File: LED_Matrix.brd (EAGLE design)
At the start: 74.6 x 29.2 mm, 48 parts, among them IC1 KF33, J1 DCJ0202, Q1 16MHz

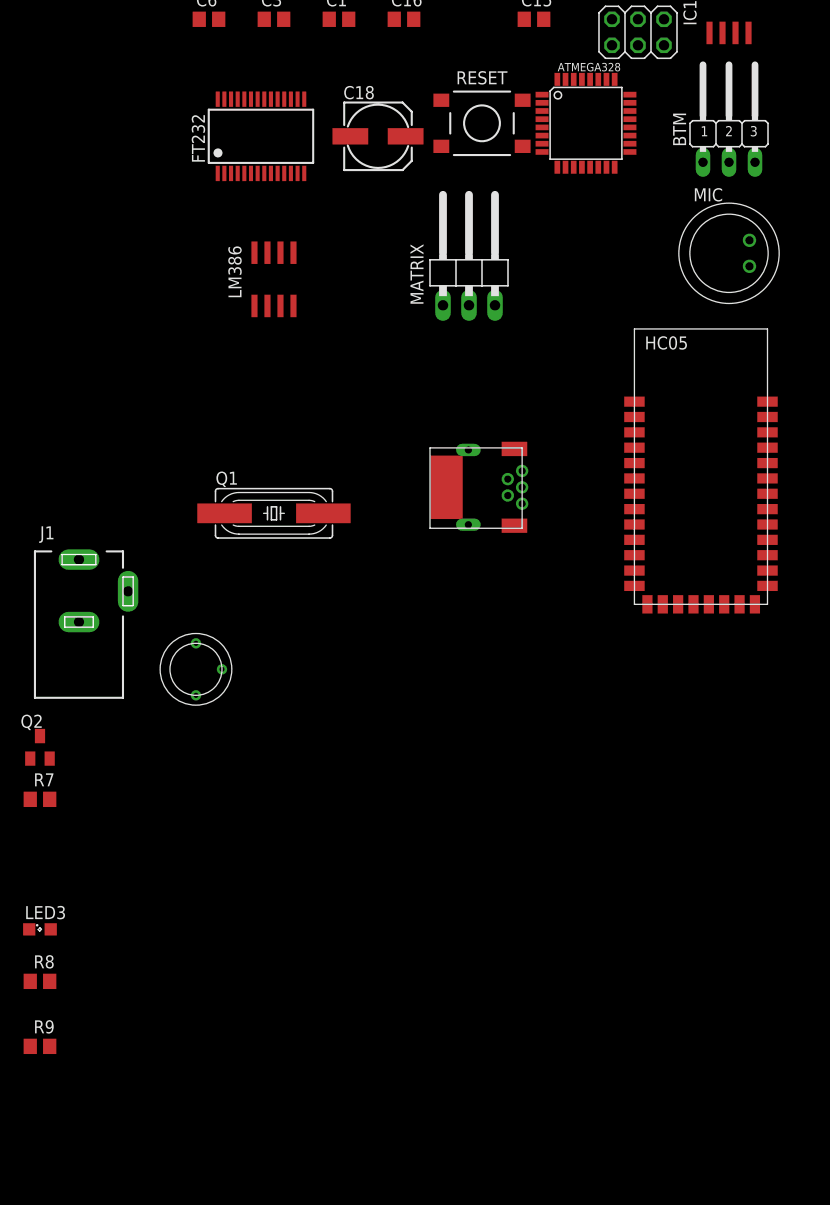
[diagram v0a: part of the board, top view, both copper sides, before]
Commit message: analog switch added
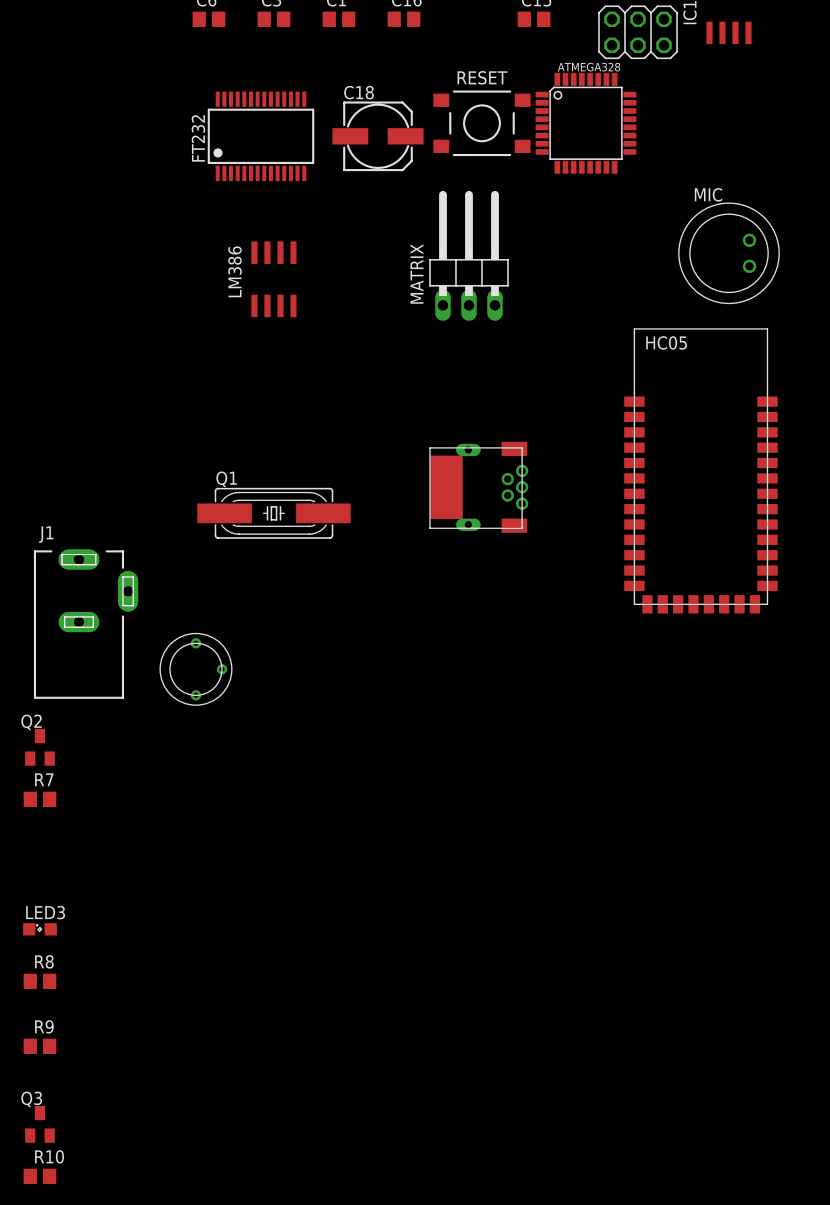
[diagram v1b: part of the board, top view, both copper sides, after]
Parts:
- removed BTM: (no value), jumper:JP2W
- added Q3: (no value), semicon-smd-ipc:SOT23
- added R10: 1k, rcl:R0805
- R7: value 10k -> 1k
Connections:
- removed net N$10: BTM.1, R4.2
- new net N$27: Q3.1, R10.2
- net BTM_MODESELECT: now also Q3.3, R10.1, R4.2; no longer BTM.2
- net GND: now also Q3.2; no longer BTM.3
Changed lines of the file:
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@@
 <element name="LM386" library="debegr92" package="SO08" value="LM386SO08" x="-62.23" y="33.02"/>
 <element name="ISP" library="pinhead" package="2X03" value="" x="-26.67" y="57.15"/>
-<element name="BTM" library="jumper" package="JP2W" value="" x="-17.78" y="45.72"/>
 <element name="LED1" library="led" package="SML0805" value="" x="-22.86" y="78.74"/>
 <element name="LED2" library="led" package="SML0805" value="" x="-29.21" y="78.74"/>
@@
 </element>
 <element name="Q2" library="semicon-smd-ipc" package="SOT23" value="" x="-85.09" y="-12.7"/>
-<element name="R7" library="rcl" package="R0805" value="10k" x="-85.09" y="-17.78"/>
+<element name="R7" library="rcl" package="R0805" value="1k" x="-85.09" y="-17.78"/>
 <element name="LED3" library="led" package="SML0805" value="" x="-85.09" y="-30.48"/>
 <element name="R8" library="rcl" package="R0805" value="470" x="-85.09" y="-35.56"/>
 <element name="R9" library="rcl" package="R0805" value="470" x="-85.09" y="-41.91"/>
+<element name="Q3" library="semicon-smd-ipc" package="SOT23" value="" x="-85.09" y="-49.53"/>
+<element name="R10" library="rcl" package="R0805" value="1k" x="-85.09" y="-54.61"/>
 </elements>
 <signals>
@@
 <contactref element="HC05" pad="21"/>
 <contactref element="R3" pad="1"/>
-<contactref element="BTM" pad="3"/>
 <contactref element="FT232" pad="25"/>
 <contactref element="FT232" pad="7"/>
@@
 <contactref element="R8" pad="1"/>
 <contactref element="R9" pad="1"/>
+<contactref element="Q3" pad="2"/>
 <contactref element="HC05" pad="22"/>
+<wire x1="-86.04" y1="-41.91" x2="-84.14" y2="-50.63" width="0" layer="19" extent="1-1"/>
 <wire x1="-86.04" y1="-35.56" x2="-86.04" y2="-41.91" width="0" layer="19" extent="1-1"/>
 <wire x1="-84.14" y1="-13.8" x2="-86.04" y2="-35.56" width="0" layer="19" extent="1-1"/>
@@
 <wire x1="-45.885" y1="46.01" x2="-37.935" y2="46.01" width="0" layer="19" extent="1-1"/>
 <wire x1="-27.4574" y1="48.66" x2="-36.0426" y2="49.46" width="0" layer="19" extent="1-1"/>
-<wire x1="-15.24" y1="44.45" x2="-17.145" y2="57.09" width="0" layer="19" extent="1-1"/>
-<wire x1="-15.78" y1="36.83" x2="-15.24" y2="44.45" width="0" layer="19" extent="1-1"/>
 <wire x1="-45.72" y1="30.48" x2="-60.325" y2="30.42" width="0" layer="19" extent="1-1"/>
+<wire x1="-15.78" y1="36.83" x2="-27.4574" y2="48.66" width="0" layer="19" extent="1-1"/>
 <wire x1="-37.99" y1="14.3" x2="-45.72" y2="30.48" width="0" layer="19" extent="1-1"/>
 <wire x1="-27.02" y1="3.07" x2="-37.99" y2="14.3" width="0" layer="19" extent="1-1"/>
@@
 </signal>
 <signal name="BTM_MODESELECT">
-<contactref element="BTM" pad="2"/>
 <contactref element="HC05" pad="34"/>
 <contactref element="ATMEGA328" pad="13"/>
-<wire x1="-31.35" y1="43.9674" x2="-17.78" y2="44.45" width="0" layer="19" extent="1-1"/>
-<wire x1="-14.02" y1="21.07" x2="-17.78" y2="44.45" width="0" layer="19" extent="1-1"/>
-</signal>
-<signal name="N$10">
-<contactref element="BTM" pad="1"/>
+<contactref element="R10" pad="1"/>
 <contactref element="R4" pad="2"/>
-<wire x1="-20.32" y1="44.45" x2="-30.8" y2="73.66" width="0" layer="19" extent="1-1"/>
+<contactref element="Q3" pad="3"/>
+<wire x1="-85.09" y1="-48.43" x2="-86.04" y2="-54.61" width="0" layer="19" extent="1-1"/>
+<wire x1="-14.02" y1="21.07" x2="-85.09" y2="-48.43" width="0" layer="19" extent="1-1"/>
+<wire x1="-31.35" y1="43.9674" x2="-14.02" y2="21.07" width="0" layer="19" extent="1-1"/>
+<wire x1="-30.8" y1="73.66" x2="-31.35" y2="43.9674" width="0" layer="19" extent="1-1"/>
 </signal>
 <signal name="N$9">
@@
 <wire x1="-14.02" y1="6.07" x2="-84.04" y2="-30.48" width="0" layer="19" extent="1-1"/>
 </signal>
+<signal name="N$27">
+<contactref element="R10" pad="2"/>
+<contactref element="Q3" pad="1"/>
+<wire x1="-86.04" y1="-50.63" x2="-84.14" y2="-54.61" width="0" layer="19" extent="1-1"/>
+</signal>
 </signals>

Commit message: return point
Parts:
- removed JRX, JTX: (no value), jumper:SJ_2
- added LEDON: (no value), led:SML0805
- added R11, R12, R13: 470, rcl:R0805
- added U$1: DG2016, Tobias:MSOP10
- C18: device rcl:153CLV-0605 -> rcl:E2,5-7
- MATRIX: device pinhead:1X03/90 -> pinhead:1X03
- moved R10 162.9 mm to (54.6, 29.2)
- moved Q3 159.6 mm to (55.9, 25.4), turned to 90 degrees
- moved R9 157.8 mm to (44.5, 48.3)
- moved R8 154.9 mm to (62.9, 10.2), flipped to the bottom, turned to 90 degrees
- moved LED3 150.7 mm to (55.9, 22.9)
- moved Q2 139.9 mm to (53.3, 7.62), turned to 270 degrees
- moved R7 137.8 mm to (49.5, 11.4)
- moved C5 115.9 mm to (48.3, 25.4), flipped to the bottom, turned to 90 degrees
- moved C19 113.1 mm to (35.6, 20.3), flipped to the bottom, turned to 270 degrees
- moved R4 112.3 mm to (57.1, 5.08), turned to 90 degrees
- moved Q1 107.8 mm to (44.5, 25.4), turned to 180 degrees
- moved LED2 107.7 mm to (55.9, 12.7)
- moved C9 105.9 mm to (54.6, 2.54), turned to 270 degrees
- moved C4 104.5 mm to (40.6, 25.4), flipped to the bottom, turned to 270 degrees
- moved LM386 104.1 mm to (38.1, 5.08)
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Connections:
- new net N$10: LEDON.C, R11.2
- new net N$26: HC05.2, R12.1, R13.2
- new net N$28: ATMEGA328.32, U$1.1
- new net N$29: ATMEGA328.1, U$1.5
- net +5V: now also LEDON.A, U$1.8
- net GND: now also R11.1, R13.1, U$1.3
- net N$12: now also U$1.10; no longer JTX.2
- net N$15: now also U$1.6; no longer JRX.2
- net RX_BTM: now also R12.2, U$1.9; no longer HC05.2, JRX.1
- net RX_FT232: now also U$1.2; no longer JRX.3
- net TX_BTM: now also U$1.7; no longer JTX.1
- net TX_FT232: now also U$1.4; no longer JTX.3
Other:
- board size 74.6 x 29.2 mm -> 74.6 x 30.5 mm

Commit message: version 2 Final
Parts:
- removed C15: 100n, rcl:C0805
- removed C16: 47n, rcl:C0805
- removed C17: 10u, rcl:C0805
- removed C18: 250u, rcl:E2,5-7
- removed C19: 470n, rcl:C0805
- removed C4, C5: 22p, rcl:C0805
- removed IC1: KF33, debegr92:SO08
- removed LEDON: (no value), led:SML0805
- removed LM386: LM386SO08, debegr92:SO08
- removed MATRIX: (no value), pinhead:1X03
- removed MIC: MIC_EMY-9765PEMY-9765P, debegr92:MIC
- removed Q1: 16MHz, crystal:HC49UP
- removed R6: 10, rcl:R0805
- removed TRIMMER: 10k, Tobias:T7YA
- removed U$1: DG2016, Tobias:MSOP10
- added D1: (no value), led:SML0805
- added DG2016: DG2016, Tobias:MSOP10
- added KF33: KF33, debegr92:SO08
- added MTX: (no value), pinhead:1X03
- added Q4: CSTCR6M00G53Z, murata-filter:CSTCR6M
- added SJ1: (no value), jumper:SJ
- moved C3 120.3 mm to (45.7, 5.40), turned to 90 degrees
- moved R5 115.0 mm to (54.3, 3.49), turned to 270 degrees
- moved C6 99.6 mm to (17.8, 8.89), flipped to the bottom, turned to 90 degrees
- moved C7 70.5 mm to (11.4, 2.54), turned to 270 degrees
- moved R13 39.7 mm to (31.1, 24.4), turned to 180 degrees
- moved R9 37.6 mm to (52.1, 11.4), turned to 180 degrees
- moved R12 36.7 mm to (31.1, 21.9), turned to 0 degrees
- moved HC05 28.0 mm to (39.4, 23.8), turned to 270 degrees
- moved R10 24.1 mm to (36.5, 13.3), turned to 270 degrees
- moved Q3 20.4 mm to (39.4, 13.3), turned to 0 degrees
- moved ATMEGA328 14.6 mm to (32.1, 6.99), turned to 0 degrees
- moved R3 14.5 mm to (52.1, 15.9), flipped to the top, turned to 180 degrees
- moved RESET 13.7 mm to (5.40, 28.3)
- moved LED3 13.1 mm to (47.9, 12.4), turned to 180 degrees
- moved C12 11.7 mm to (22.9, 12.7), flipped to the top, turned to 0 degrees
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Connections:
- removed net N$16: C19.1, MIC.TERMINAL1, TRIMMER.B
- removed net N$17: C17.2, LM386.8
- removed net N$18: C16.2, R6.1
- removed net N$20: C17.1, LM386.1
- removed net N$21: C16.1, C18.+, LM386.5
- removed net N$22: C19.2, LM386.3
- net +3V3: now also KF33.1; no longer IC1.1
- net +5V: now also D1.A, DG2016.8, KF33.8, MTX.3, SJ1.2; no longer IC1.8, LEDON.A, LM386.6, MATRIX.3, TRIMMER.A, U$1.8, USB.5, USB.GND, USB.GND1, USB.GND3, USB.GND4, USB.GND5
- net AUDIO_IN: no longer C18.-
- net GND: now also DG2016.3, KF33.2, KF33.3, KF33.6, KF33.7, MTX.1, Q4.2, USB.5, USB.GND, USB.GND1, USB.GND3, USB.GND4, USB.GND5; no longer C15.2, C4.1, C5.1, IC1.2, IC1.3, IC1.6, IC1.7, LM386.2, LM386.4, MATRIX.1, MIC.TERMINAL2, R6.2, TRIMMER.C, U$1.3, USB.1
- net N$10: now also D1.C; no longer LEDON.C
- net N$12: now also DG2016.10; no longer U$1.10
- net N$15: now also DG2016.6; no longer U$1.6
- net N$2: now also SJ1.1, USB.1; no longer C15.1, LM386.7
- net N$28: now also DG2016.1; no longer U$1.1
- net N$29: now also DG2016.5; no longer U$1.5
- net N$3: now also Q4.1; no longer C4.2, Q1.1
- net N$4: now also MTX.2; no longer MATRIX.2
- net N$7: now also Q4.3; no longer C5.2, Q1.2
- net RX_BTM: now also DG2016.9; no longer U$1.9
- net RX_FT232: now also DG2016.2; no longer U$1.2
- net TX_BTM: now also DG2016.7; no longer U$1.7
- net TX_FT232: now also DG2016.4; no longer U$1.4
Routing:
- net GND: track 0.00 -> 235.4 mm, vias 0 -> 2
- net +5V: track 0.00 -> 138.5 mm, vias 0 -> 3
- net RESET: track 0.00 -> 80.2 mm, vias 0 -> 2
- net +3V3: track 0.00 -> 72.8 mm, vias 0 -> 4
- net MATRIX_DATA: track 0.00 -> 62.0 mm, vias 0 -> 1
- net BTM_MODESELECT: track 0.00 -> 49.5 mm, vias 0 -> 4
- net N$23: track 0.00 -> 49.2 mm, vias 0 -> 4
- net TX_BTM: track 0.00 -> 23.7 mm, vias 0 -> 2
- net N$26: track 0.00 -> 19.0 mm, vias 0 -> 1
- net N$24: track 0.00 -> 18.2 mm
- net TX_FT232: track 0.00 -> 16.4 mm
- net BTM_RST: track 0.00 -> 16.4 mm
- net N$4: track 0.00 -> 15.1 mm
- net RX_FT232: track 0.00 -> 14.8 mm
- net RX_BTM: track 0.00 -> 14.4 mm, vias 0 -> 1
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- added copper zone on layer 1, net GND
- added copper zone on layer 16, net GND
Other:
- board size 74.6 x 30.5 mm -> 56.2 x 32.1 mm
- board text added: "D"
- board text added: "GND"
- board text added: "V+"

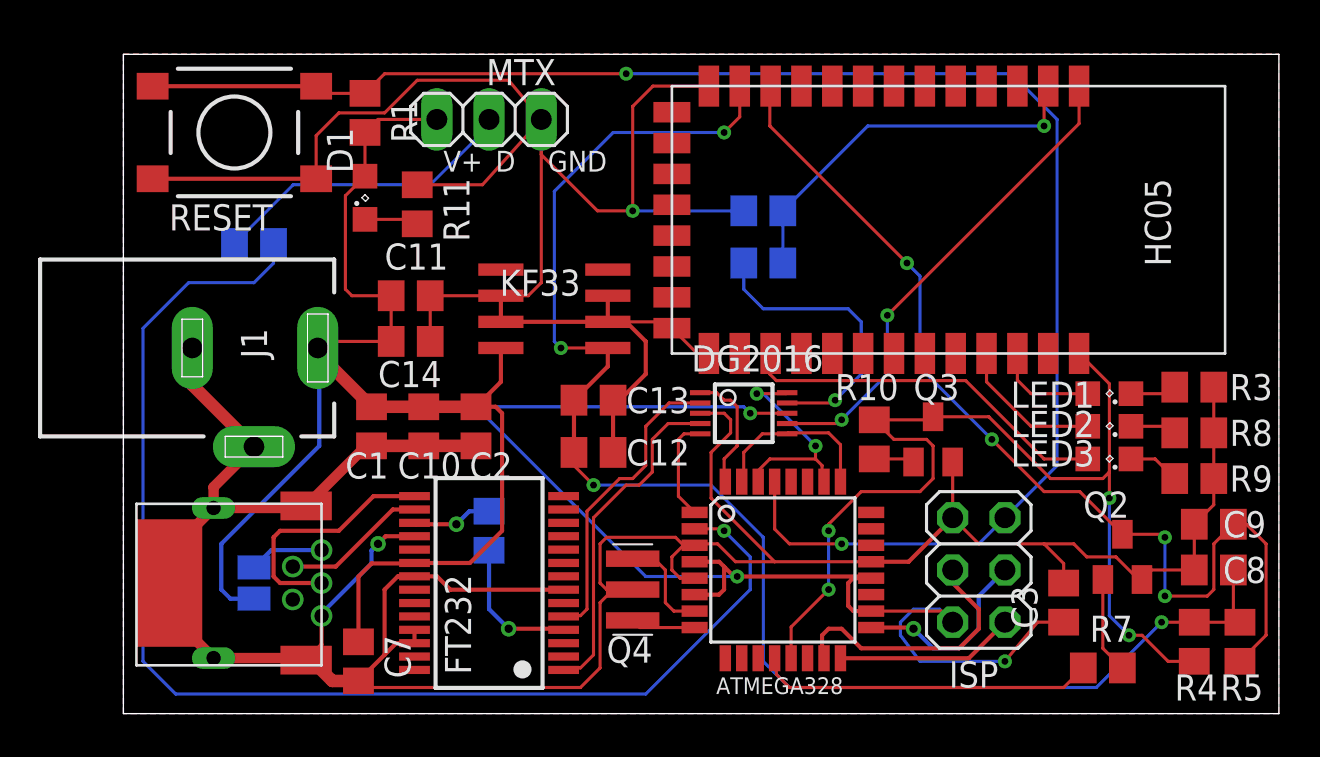
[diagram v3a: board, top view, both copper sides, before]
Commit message: Audo in added
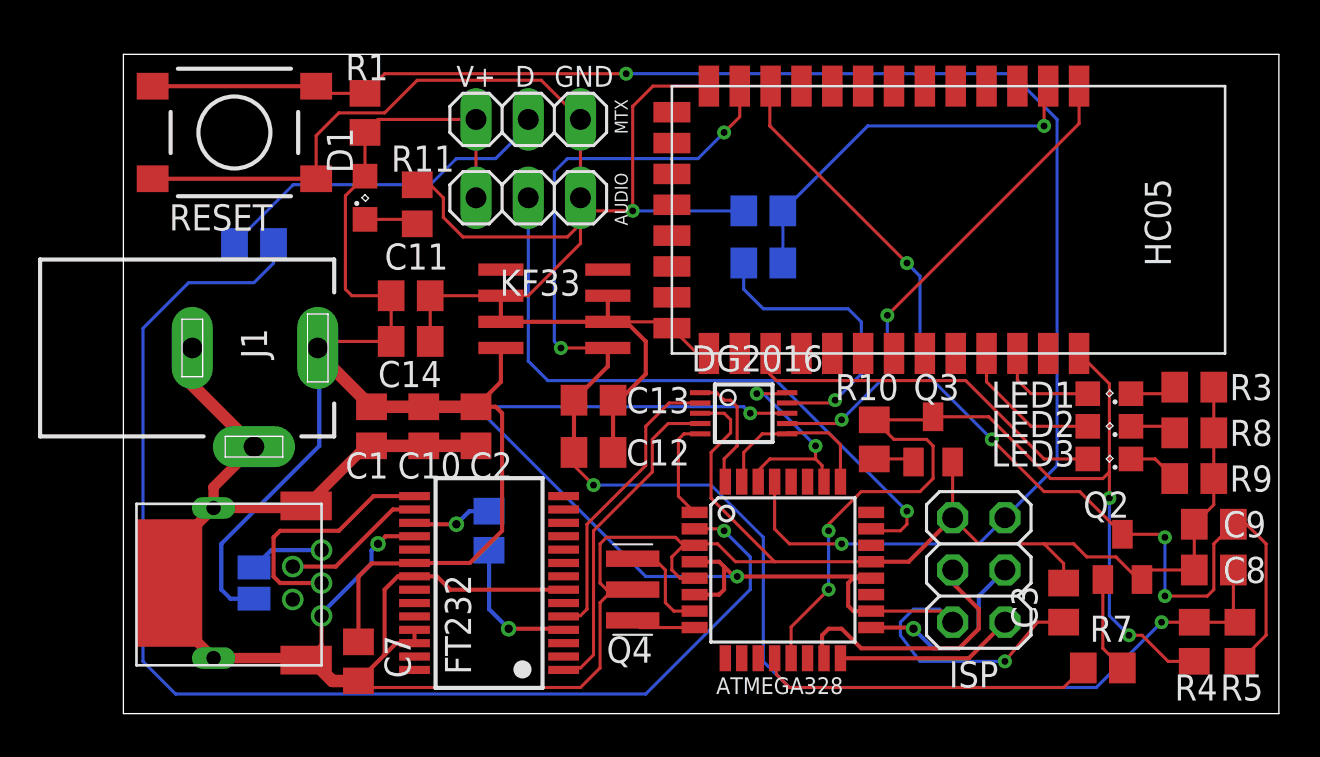
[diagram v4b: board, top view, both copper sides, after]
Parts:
- added AUDIO: (no value), pinhead:1X03
- moved MTX 1.90 mm to (19.7, 28.9)
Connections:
- net +5V: now also AUDIO.1
- net AUDIO_IN: now also AUDIO.2
- net GND: now also AUDIO.3
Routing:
- net AUDIO_IN: track 0.00 -> 31.9 mm, vias 0 -> 1
- net +5V: track 138.5 -> 144.3 mm
- net N$4: track 15.1 -> 17.0 mm
- net +3V3: track 72.8 -> 73.4 mm
- removed copper zone on layer 1, net GND
- removed copper zone on layer 16, net GND
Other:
- board text added: "LEDmatrix Tobias Nuß 05.11.2015"

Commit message: added some GND Vias and Polygons
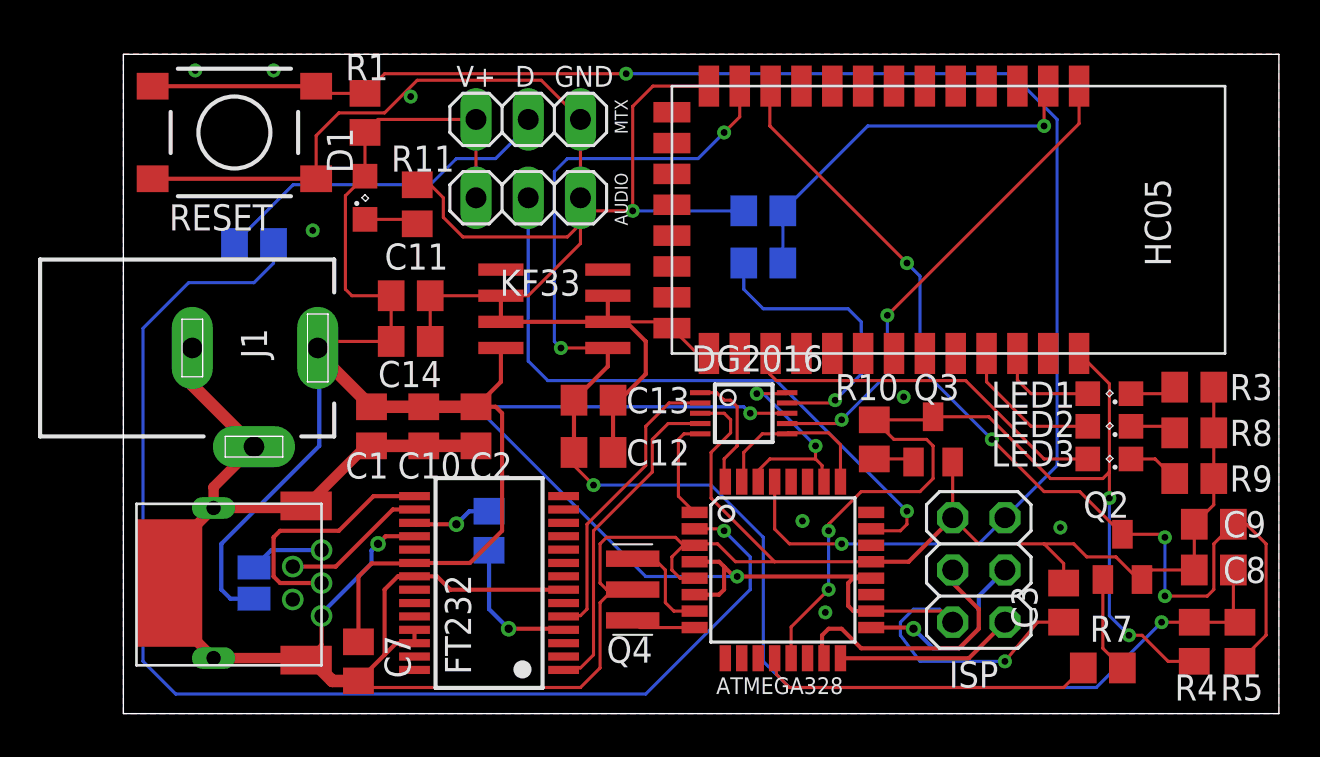
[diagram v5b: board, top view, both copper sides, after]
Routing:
- net GND: vias 2 -> 10
- added copper zone on layer 1, net GND
- added copper zone on layer 16, net GND
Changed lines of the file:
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@@
 <wire x1="19.685" y1="20.32" x2="22.225" y2="22.86" width="0.1524" layer="1"/>
 <wire x1="22.225" y1="22.86" x2="22.225" y2="23.8125" width="0.1524" layer="1"/>
-<wire x1="28.0494" y1="14.605" x2="27.9" y2="17.5125" width="0" layer="19" extent="1-1"/>
+<via x="9.2075" y="23.495" extent="1-16" drill="0.3302"/>
+<polygon width="0.1524" layer="1">
+<vertex x="0" y="32.0675"/>
+<vertex x="56.1975" y="32.0675"/>
+<vertex x="56.1975" y="0"/>
+<vertex x="0" y="0"/>
+</polygon>
+<polygon width="0.1524" layer="16">
+<vertex x="0" y="32.0675"/>
+<vertex x="56.1975" y="32.0675"/>
+<vertex x="56.1975" y="0"/>
+<vertex x="0" y="0"/>
+</polygon>
+<via x="3.4925" y="31.27375" extent="1-16" drill="0.3302"/>
+<via x="7.3025" y="31.27375" extent="1-16" drill="0.3302"/>
+<via x="13.97" y="30.00375" extent="1-16" drill="0.3302"/>
+<via x="33.02" y="9.36625" extent="1-16" drill="0.3302"/>
+<via x="34.13125" y="4.92125" extent="1-16" drill="0.3302"/>
+<via x="37.94125" y="15.39875" extent="1-16" drill="0.3302"/>
+<via x="45.56125" y="9.04875" extent="1-16" drill="0.3302"/>
 </signal>
 <signal name="N$7">
